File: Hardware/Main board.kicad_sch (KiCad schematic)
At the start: 38 parts, among them U1 ESP32-S3, Y1 R940000171

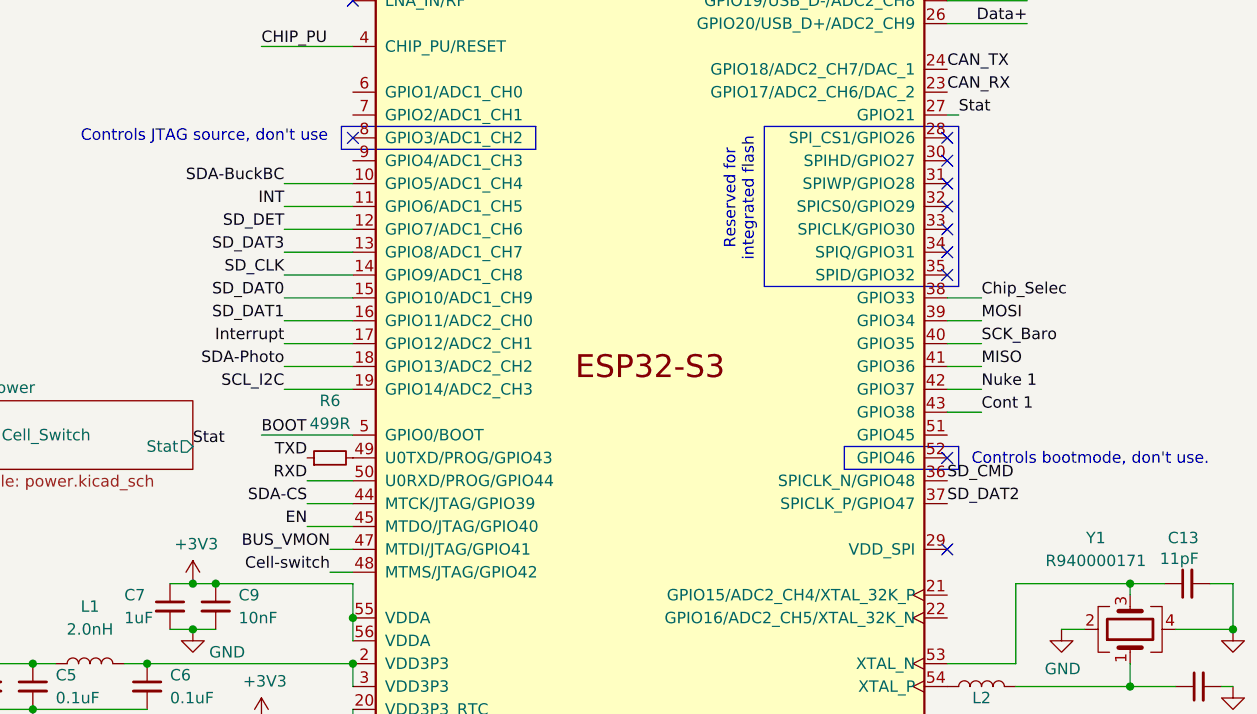
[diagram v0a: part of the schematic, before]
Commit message: Traces connected + rejigging
Most DRC errors taken care of
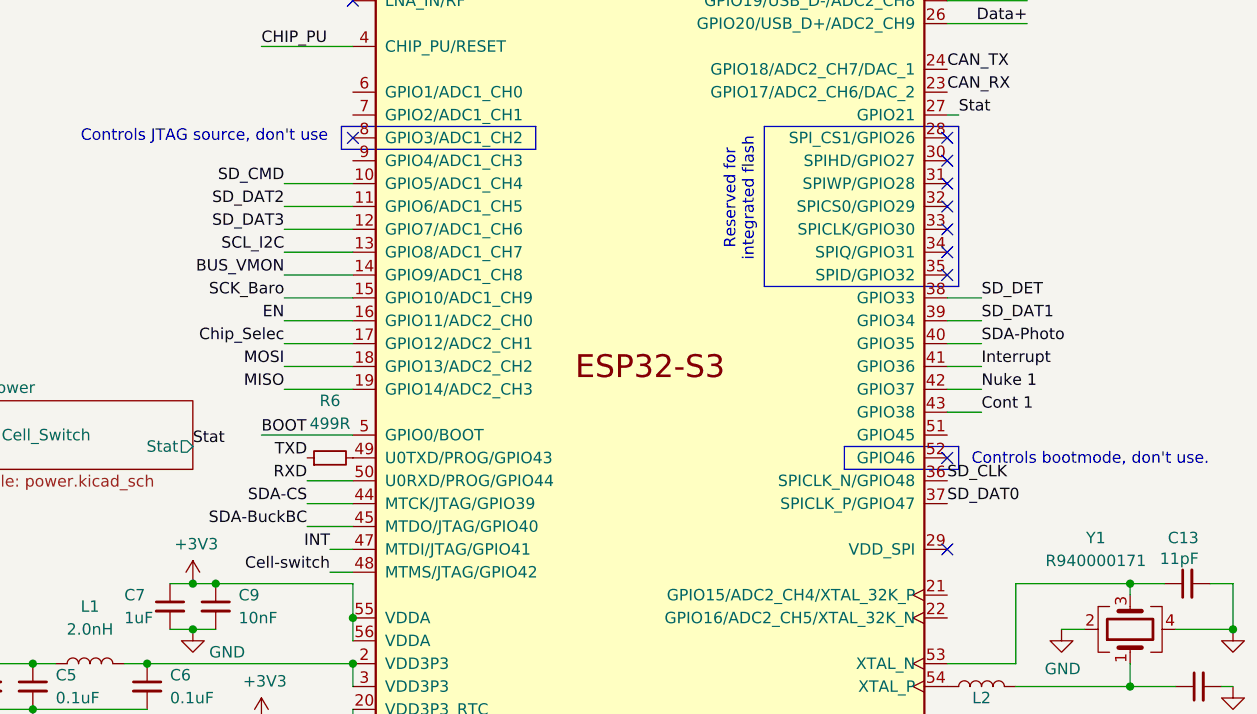
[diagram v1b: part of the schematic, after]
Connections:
- net BUS_VMON: now also U1.14 (GPIO9/ADC1_CH8); no longer U1.47 (MTDI/JTAG/GPIO41)
- net Chip_Selec: now also U1.17 (GPIO12/ADC2_CH1); no longer U1.38 (GPIO33)
- net EN: now also U1.16 (GPIO11/ADC2_CH0); no longer U1.45 (MTDO/JTAG/GPIO40)
- net INT: now also U1.47 (MTDI/JTAG/GPIO41); no longer U1.11 (GPIO6/ADC1_CH5)
- net Interrupt : now also U1.41 (GPIO36); no longer U1.17 (GPIO12/ADC2_CH1)
- net MISO: now also U1.19 (GPIO14/ADC2_CH3); no longer U1.41 (GPIO36)
- net MOSI: now also U1.18 (GPIO13/ADC2_CH2); no longer U1.39 (GPIO34)
- net SCK_Baro: now also U1.15 (GPIO10/ADC1_CH9); no longer U1.40 (GPIO35)
- net SCL_I2C: now also U1.13 (GPIO8/ADC1_CH7); no longer U1.19 (GPIO14/ADC2_CH3)
- net SDA-BuckBC: now also U1.45 (MTDO/JTAG/GPIO40); no longer U1.10 (GPIO5/ADC1_CH4)
- net SDA-Photo: now also U1.40 (GPIO35); no longer U1.18 (GPIO13/ADC2_CH2)
- net SD_CLK: now also U1.36 (SPICLK_N/GPIO48); no longer U1.14 (GPIO9/ADC1_CH8)
- net SD_CMD: now also U1.10 (GPIO5/ADC1_CH4); no longer U1.36 (SPICLK_N/GPIO48)
- net SD_DAT0: now also U1.37 (SPICLK_P/GPIO47); no longer U1.15 (GPIO10/ADC1_CH9)
- net SD_DAT1: now also U1.39 (GPIO34); no longer U1.16 (GPIO11/ADC2_CH0)
- net SD_DAT2: now also U1.11 (GPIO6/ADC1_CH5); no longer U1.37 (SPICLK_P/GPIO47)
- net SD_DAT3: now also U1.12 (GPIO7/ADC1_CH6); no longer U1.13 (GPIO8/ADC1_CH7)
- net SD_DET: now also U1.38 (GPIO33); no longer U1.12 (GPIO7/ADC1_CH6)
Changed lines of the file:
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@@
+		)
+	)
+	(label "EN"
+		(at 62.23 97.79 180)
+		(effects
+			(font
+				(size 1.27 1.27)
+			)
+			(justify right bottom)
 		)
 	)
@@
 		)
 	)
-	(label "SCK_Baro"
-		(at 139.7 100.33 0)
-		(effects
-			(font
-				(size 1.27 1.27)
-			)
-			(justify left bottom)
-		)
-	)
-	(label "Chip_Selec"
-		(at 139.7 95.25 0)
-		(effects
-			(font
-				(size 1.27 1.27)
-			)
-			(justify left bottom)
-		)
-	)
 	(label "CHIP_PU"
 		(at 36.83 165.1 180)
@@
 		)
 	)
-	(label "SDA-BuckBC"
-		(at 62.23 82.55 180)
-		(effects
-			(font
-				(size 1.27 1.27)
-			)
-			(justify right bottom)
-		)
-	)
 	(label "Interrupt "
 		(at 226.06 92.71 0)
@@
 			)
 			(justify right bottom)
+		)
+	)
+	(label "SD_DAT1"
+		(at 139.7 97.79 0)
+		(effects
+			(font
+				(size 1.27 1.27)
+			)
+			(justify left bottom)
 		)
 	)
@@
 		)
 	)
-	(label "MOSI"
-		(at 139.7 97.79 0)
-		(effects
-			(font
-				(size 1.27 1.27)
-			)
-			(justify left bottom)
-		)
-	)
 	(label "RXD"
 		(at 30.48 59.69 0)
@@
 		)
 	)
+	(label "INT"
+		(at 67.31 123.19 180)
+		(effects
+			(font
+				(size 1.27 1.27)
+			)
+			(justify right bottom)
+		)
+	)
+	(label "SD_DAT2"
+		(at 62.23 85.09 180)
+		(effects
+			(font
+				(size 1.27 1.27)
+			)
+			(justify right bottom)
+		)
+	)
 	(label "SD_CMD"
 		(at 248.92 127 180)
@@
 		)
 	)
-	(label "SD_DAT3"
-		(at 62.23 90.17 180)
+	(label "SCK_Baro"
+		(at 62.23 95.25 180)
+		(effects
+			(font
+				(size 1.27 1.27)
+			)
+			(justify right bottom)
+		)
+	)
+	(label "MOSI"
+		(at 62.23 102.87 180)
+		(effects
+			(font
+				(size 1.27 1.27)
+			)
+			(justify right bottom)
+		)
+	)
+	(label "Chip_Selec"
+		(at 62.23 100.33 180)
 		(effects
 			(font
@@
 		)
 	)
-	(label "Interrupt "
-		(at 62.23 100.33 180)
-		(effects
-			(font
-				(size 1.27 1.27)
-			)
-			(justify right bottom)
-		)
-	)
 	(label "TXD"
 		(at 30.48 54.61 0)
@@
 		)
 	)
-	(label "SD_CMD"
-		(at 135.89 115.57 0)
-		(effects
-			(font
-				(size 1.27 1.27)
-			)
-			(justify left bottom)
+	(label "SCL_I2C"
+		(at 62.23 90.17 180)
+		(effects
+			(font
+				(size 1.27 1.27)
+			)
+			(justify right bottom)
+		)
+	)
+	(label "MISO"
+		(at 62.23 105.41 180)
+		(effects
+			(font
+				(size 1.27 1.27)
+			)
+			(justify right bottom)
 		)
 	)
@@
 		)
 	)
-	(label "SD_DAT2"
-		(at 135.89 118.11 0)
-		(effects
-			(font
-				(size 1.27 1.27)
-			)
-			(justify left bottom)
-		)
-	)
 	(label "SD_DAT0"
 		(at 248.92 134.62 180)
@@
 		)
 	)
+	(label "SD_DET"
+		(at 139.7 95.25 0)
+		(effects
+			(font
+				(size 1.27 1.27)
+			)
+			(justify left bottom)
+		)
+	)
 	(label "BUS_VMON"
 		(at 237.49 59.69 0)
@@
 		)
 	)
-	(label "SD_DAT1"
-		(at 62.23 97.79 180)
-		(effects
-			(font
-				(size 1.27 1.27)
-			)
-			(justify right bottom)
-		)
-	)
-	(label "INT"
-		(at 62.23 85.09 180)
-		(effects
-			(font
-				(size 1.27 1.27)
-			)
-			(justify right bottom)
-		)
-	)
 	(label "BOOT"
 		(at 68.58 165.1 180)
@@
 		)
 	)
-	(label "SD_CLK"
-		(at 62.23 92.71 180)
-		(effects
-			(font
-				(size 1.27 1.27)
-			)
-			(justify right bottom)
-		)
-	)
-	(label "SD_DAT0"
-		(at 62.23 95.25 180)
-		(effects
-			(font
-				(size 1.27 1.27)
-			)
-			(justify right bottom)
-		)
-	)
 	(label "SDA-Photo"
 		(at 226.06 88.9 0)
@@
 			)
 			(justify right bottom)
+		)
+	)
+	(label "Interrupt "
+		(at 139.7 102.87 0)
+		(effects
+			(font
+				(size 1.27 1.27)
+			)
+			(justify left bottom)
+		)
+	)
+	(label "SD_CLK"
+		(at 135.89 115.57 0)
+		(effects
+			(font
+				(size 1.27 1.27)
+			)
+			(justify left bottom)
 		)
 	)
@@
 		)
 	)
+	(label "SD_DAT0"
+		(at 135.89 118.11 0)
+		(effects
+			(font
+				(size 1.27 1.27)
+			)
+			(justify left bottom)
+		)
+	)
 	(label "CAN_TX"
 		(at 13.97 30.48 0)
@@
 		)
 	)
-	(label "MISO"
-		(at 139.7 102.87 0)
-		(effects
-			(font
-				(size 1.27 1.27)
-			)
-			(justify left bottom)
+	(label "SDA-BuckBC"
+		(at 64.77 120.65 180)
+		(effects
+			(font
+				(size 1.27 1.27)
+			)
+			(justify right bottom)
 		)
 	)
@@
 		)
 	)
-	(label "SD_DET"
-		(at 62.23 87.63 180)
-		(effects
-			(font
-				(size 1.27 1.27)
-			)
-			(justify right bottom)
-		)
-	)
 	(label "CAN_RX"
 		(at 135.89 72.39 0)
@@
 		)
 	)
-	(label "EN"
-		(at 64.77 120.65 180)
-		(effects
-			(font
-				(size 1.27 1.27)
-			)
-			(justify right bottom)
-		)
-	)
 	(label "Cont 1"
 		(at 200.66 31.75 180)
@@
 		)
 	)
-	(label "SCL_I2C"
-		(at 62.23 105.41 180)
+	(label "SD_DAT3"
+		(at 62.23 87.63 180)
 		(effects
 			(font
@@
 		)
 	)
-	(label "BUS_VMON"
-		(at 67.31 123.19 180)
-		(effects
-			(font
-				(size 1.27 1.27)
-			)
-			(justify right bottom)
-		)
-	)
-	(label "SDA-Photo"
-		(at 62.23 102.87 180)
-		(effects
-			(font
-				(size 1.27 1.27)
-			)
-			(justify right bottom)
-		)
-	)
 	(label "SCL_I2C"
 		(at 237.49 55.88 0)
@@
 		)
 	)
+	(label "SDA-Photo"
+		(at 139.7 100.33 0)
+		(effects
+			(font
+				(size 1.27 1.27)
+			)
+			(justify left bottom)
+		)
+	)
 	(label "SDA-CS"
 		(at 237.49 63.5 0)
@@
 			)
 			(justify left bottom)
+		)
+	)
+	(label "SD_CMD"
+		(at 62.23 82.55 180)
+		(effects
+			(font
+				(size 1.27 1.27)
+			)
+			(justify right bottom)
 		)
 	)
@@
 		)
 	)
+	(label "BUS_VMON"
+		(at 62.23 92.71 180)
+		(effects
+			(font
+				(size 1.27 1.27)
+			)
+			(justify right bottom)
+		)
+	)

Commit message: Major changes made to layout
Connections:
- net BUS_VMON is gone; now on net Stat: U1.14 (GPIO9/ADC1_CH8)
- net Stat: no longer U1.27 (GPIO21)
- net EN: no longer names the net of U1.16 (GPIO11/ADC2_CH0)
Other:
- sheet Voltage Regulation ports: added none; removed BUS_VMON, EN
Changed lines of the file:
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@@
 	(wire
 		(pts
+			(xy 62.23 92.71) (xy 69.85 92.71)
+		)
+		(stroke
+			(width 0)
+			(type default)
+		)
+	)
+	(wire
+		(pts
 			(xy 69.85 135.89) (xy 69.85 138.43)
 		)
@@
 	(wire
 		(pts
-			(xy 237.49 59.69) (xy 236.22 59.69)
-		)
-		(stroke
-			(width 0)
-			(type default)
-		)
-	)
-	(wire
-		(pts
 			(xy 69.85 130.81) (xy 69.85 133.35)
 		)
@@
 	(wire
 		(pts
-			(xy 201.93 55.88) (xy 203.2 55.88)
-		)
-		(stroke
-			(width 0)
-			(type default)
-		)
-	)
-	(wire
-		(pts
 			(xy 17.78 21.59) (xy 22.86 21.59)
 		)
@@
 	(wire
 		(pts
-			(xy 62.23 92.71) (xy 69.85 92.71)
-		)
-		(stroke
-			(width 0)
-			(type default)
-		)
-	)
-	(wire
-		(pts
 			(xy 161.29 138.43) (xy 156.21 138.43)
 		)
@@
 	(wire
 		(pts
-			(xy 62.23 97.79) (xy 69.85 97.79)
-		)
-		(stroke
-			(width 0)
-			(type default)
-		)
-	)
-	(wire
-		(pts
 			(xy 53.34 191.77) (xy 45.72 191.77)
 		)
@@
 	(wire
 		(pts
-			(xy 137.16 74.93) (xy 135.89 74.93)
-		)
-		(stroke
-			(width 0)
-			(type default)
-		)
-	)
-	(wire
-		(pts
 			(xy 20.32 135.89) (xy 29.21 135.89)
 		)
@@
 		)
 	)
-	(label "EN"
-		(at 62.23 97.79 180)
-		(effects
-			(font
-				(size 1.27 1.27)
-			)
-			(justify right bottom)
-		)
-	)
 	(label "Chip_Selec"
 		(at 201.93 85.09 180)
@@
 		)
 	)
-	(label "Stat"
-		(at 137.16 74.93 0)
-		(effects
-			(font
-				(size 1.27 1.27)
-			)
-			(justify left bottom)
-		)
-	)
 	(label "Data+"
 		(at 99.06 160.02 0)
@@
 		)
 	)
-	(label "EN"
-		(at 201.93 55.88 180)
-		(effects
-			(font
-				(size 1.27 1.27)
-			)
-			(justify right bottom)
-		)
-	)
 	(label "SD_DET"
 		(at 139.7 95.25 0)
@@
 		)
 	)
-	(label "BUS_VMON"
-		(at 237.49 59.69 0)
-		(effects
-			(font
-				(size 1.27 1.27)
-			)
-			(justify left bottom)
-		)
-	)
 	(label "BOOT"
 		(at 68.58 165.1 180)
@@
 		)
 	)
+	(label "Stat"
+		(at 62.23 92.71 180)
+		(effects
+			(font
+				(size 1.27 1.27)
+			)
+			(justify right bottom)
+		)
+	)
 	(label "SDA-CS"
 		(at 237.49 63.5 0)
@@
 		)
 	)
-	(label "BUS_VMON"
-		(at 62.23 92.71 180)
-		(effects
-			(font
-				(size 1.27 1.27)
-			)
-			(justify right bottom)
-		)
-	)
 	(label "SD_DAT3"
 		(at 248.92 129.54 180)
@@
 			)
 		)
-		(pin "BUS_VMON" output
-			(at 236.22 59.69 0)
-			(effects
-				(font
-					(size 1.27 1.27)
-				)
-				(justify right)
-			)
-		)
-		(pin "EN" input
-			(at 203.2 55.88 180)
-			(effects
-				(font
-					(size 1.27 1.27)
-				)
-				(justify left)
-			)
-		)

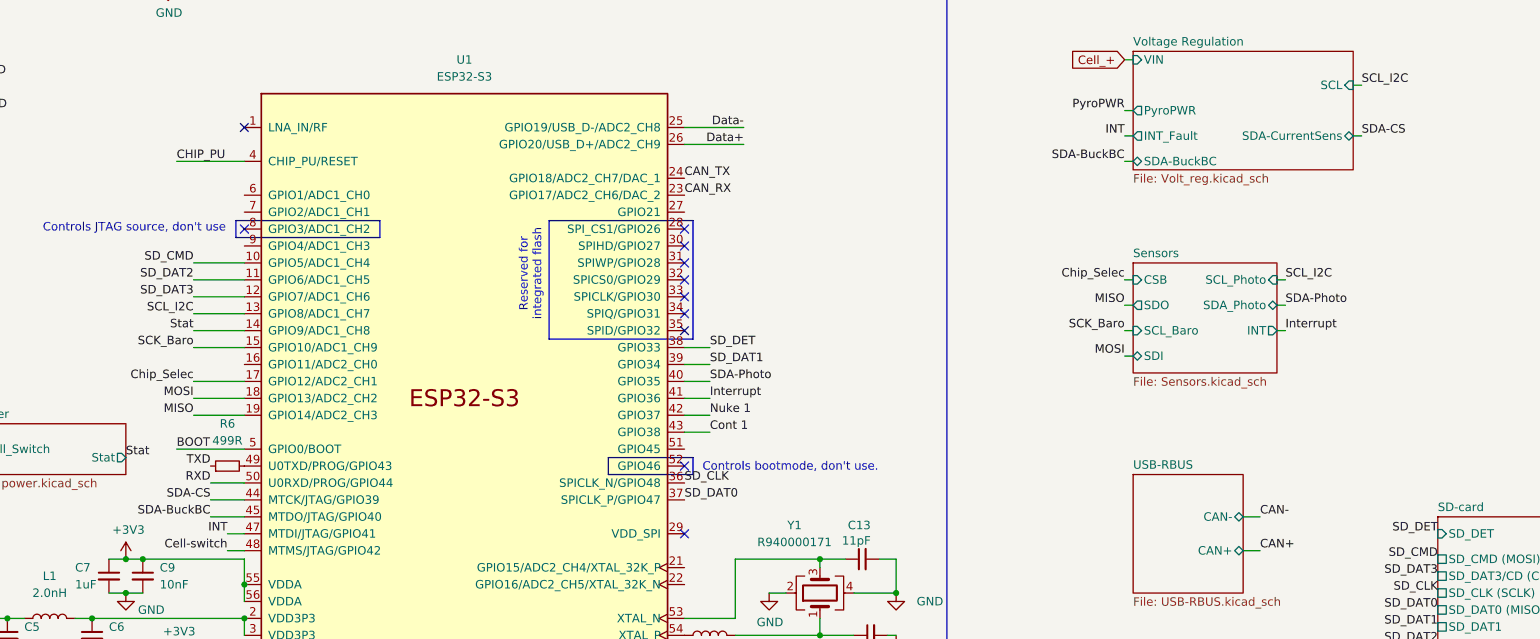
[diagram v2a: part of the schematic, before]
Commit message: I2C 'bus' sorted
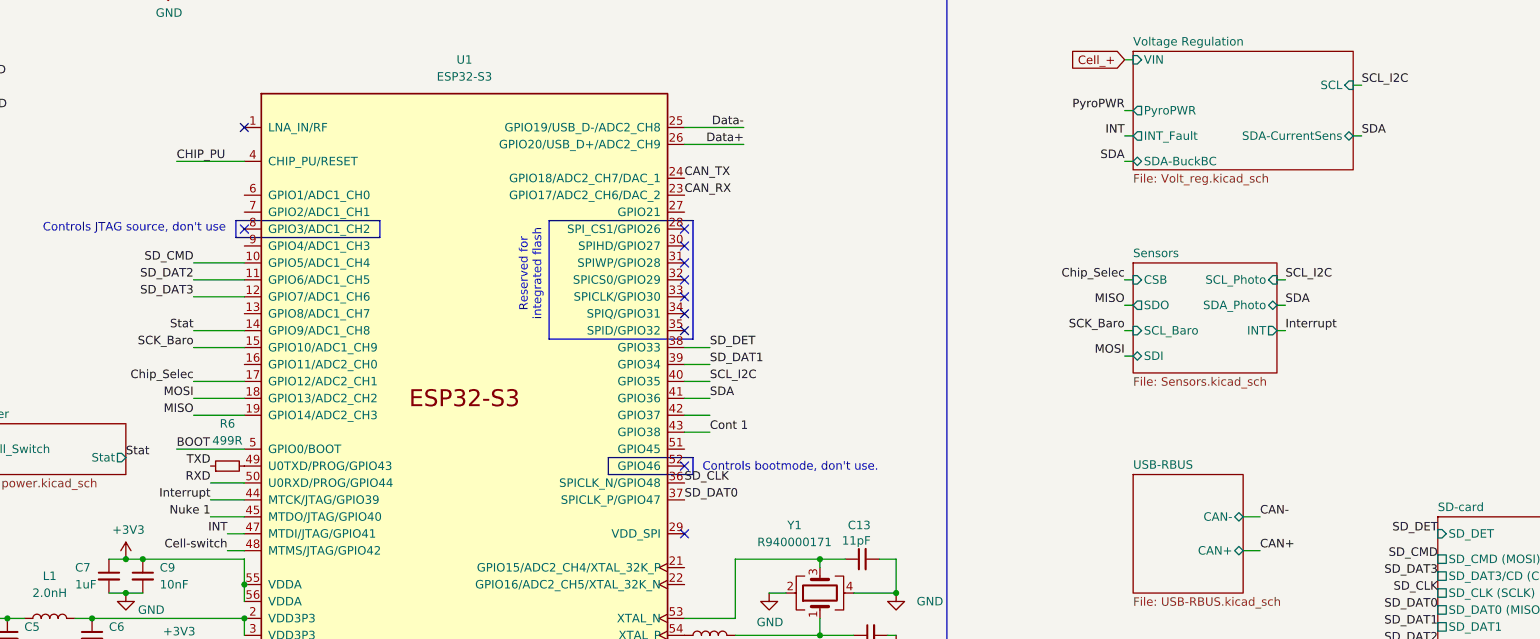
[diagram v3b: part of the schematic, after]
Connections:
- net SDA-BuckBC is gone; now on net Nuke 1: U1.45 (MTDO/JTAG/GPIO40)
- net SDA-CS is gone; now on net Interrupt : U1.44 (MTCK/JTAG/GPIO39)
- net SDA-Photo is gone; now on net SCL_I2C: U1.40 (GPIO35)
- net Interrupt : no longer U1.41 (GPIO36)
- net Nuke 1: no longer U1.42 (GPIO37)
- net SCL_I2C: no longer U1.13 (GPIO8/ADC1_CH7)
- new net SDA: U1.41 (GPIO36)
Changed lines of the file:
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@@
-	(wire
-		(pts
-			(xy 62.23 90.17) (xy 69.85 90.17)
-		)
-		(stroke
-			(width 0)
-			(type default)
-		)
-	)
 	(wire
 		(pts
@@
 		)
 	)
-	(label "SDA-BuckBC"
+	(label "SDA"
 		(at 201.93 67.31 180)
 		(effects
@@
 		)
 	)
+	(label "Interrupt "
+		(at 64.77 118.11 180)
+		(effects
+			(font
+				(size 1.27 1.27)
+			)
+			(justify right bottom)
+		)
+	)
 	(label "TXD"
 		(at 30.48 54.61 0)
@@
 		)
 	)
-	(label "SCL_I2C"
-		(at 62.23 90.17 180)
-		(effects
-			(font
-				(size 1.27 1.27)
-			)
-			(justify right bottom)
-		)
-	)
 	(label "MISO"
 		(at 62.23 105.41 180)
@@
 		)
 	)
+	(label "SCL_I2C"
+		(at 139.7 100.33 0)
+		(effects
+			(font
+				(size 1.27 1.27)
+			)
+			(justify left bottom)
+		)
+	)
 	(label "BOOT"
 		(at 68.58 165.1 180)
@@
 		)
 	)
-	(label "SDA-Photo"
+	(label "Nuke 1"
+		(at 64.77 120.65 180)
+		(effects
+			(font
+				(size 1.27 1.27)
+			)
+			(justify right bottom)
+		)
+	)
+	(label "SDA"
+		(at 139.7 102.87 0)
+		(effects
+			(font
+				(size 1.27 1.27)
+			)
+			(justify left bottom)
+		)
+	)
+	(label "SDA"
 		(at 226.06 88.9 0)
 		(effects
@@
 			)
 			(justify right bottom)
-		)
-	)
-	(label "Interrupt "
-		(at 139.7 102.87 0)
-		(effects
-			(font
-				(size 1.27 1.27)
-			)
-			(justify left bottom)
 		)
 	)
@@
 		)
 	)
-	(label "SDA-BuckBC"
-		(at 64.77 120.65 180)
-		(effects
-			(font
-				(size 1.27 1.27)
-			)
-			(justify right bottom)
-		)
-	)
 	(label "CHIP_PU"
 		(at 59.69 67.31 0)
@@
 		)
 	)
-	(label "Nuke 1"
-		(at 139.7 105.41 0)
-		(effects
-			(font
-				(size 1.27 1.27)
-			)
-			(justify left bottom)
-		)
-	)
 	(label "MOSI"
 		(at 201.93 96.52 180)
@@
 		)
 	)
-	(label "SDA-CS"
-		(at 64.77 118.11 180)
-		(effects
-			(font
-				(size 1.27 1.27)
-			)
-			(justify right bottom)
-		)
-	)
 	(label "SD_DAT3"
 		(at 62.23 87.63 180)
@@
 		)
 	)
-	(label "SDA-Photo"
-		(at 139.7 100.33 0)
-		(effects
-			(font
-				(size 1.27 1.27)
-			)
-			(justify left bottom)
-		)
-	)
 	(label "Stat"
 		(at 62.23 92.71 180)
@@
 		)
 	)
-	(label "SDA-CS"
+	(label "SDA"
 		(at 237.49 63.5 0)
 		(effects
